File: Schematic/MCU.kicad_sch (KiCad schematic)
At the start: 21 parts, among them IC3 STM32H743VIT6, SW1 TS24CA, Y1 8MHz

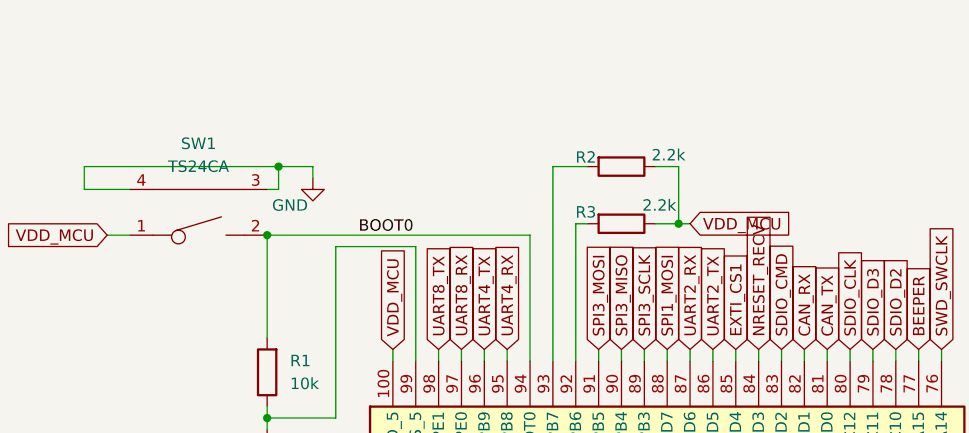
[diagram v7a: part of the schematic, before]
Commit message: update schematic after reviewing some footprints
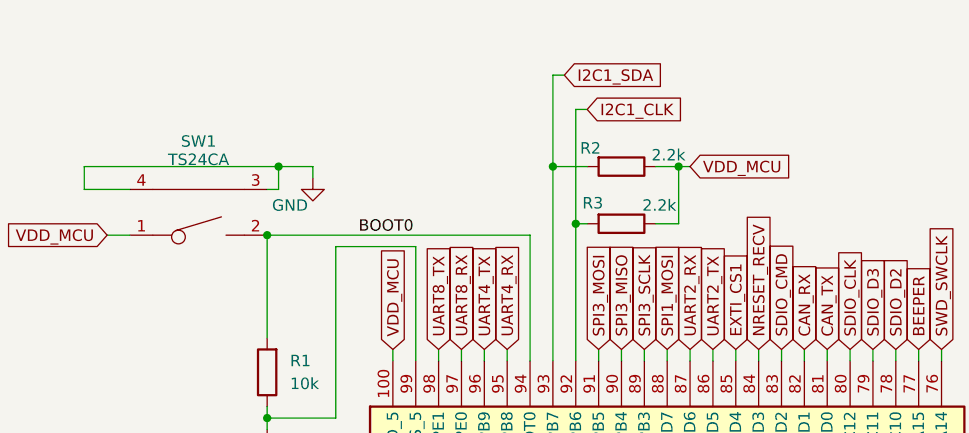
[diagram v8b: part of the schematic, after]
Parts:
- C1, C53: MPN CL10A225KB8NNNC -> (none); Manufacturer SAMSUNG -> (none)
- C2, C5, C6, C7, C8, C9: MPN 0603B104K500NT -> (none); Manufacturer FH -> (none)
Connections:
- net I2C1_SDA: now reaches IC3.93 (PB7), R2.2
- net I2C1_CLK: now reaches IC3.92 (PB6), R3.2
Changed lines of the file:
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@@
 	)
 	(junction
+		(at 88.9 29.21)
+		(diameter 0)
+		(color 0 0 0 0)
+	)
+	(junction
 		(at 58.42 29.21)
 		(diameter 0)
@@
 	)
 	(junction
+		(at 102.87 29.21)
+		(diameter 0)
+		(color 0 0 0 0)
+	)
+	(junction
 		(at 220.98 30.48)
 		(diameter 0)
@@
 	)
 	(junction
+		(at 91.44 35.56)
+		(diameter 0)
+		(color 0 0 0 0)
+	)
+	(junction
 		(at 127 158.75)
 		(diameter 0)
@@
 	)
 	(junction
-		(at 102.87 35.56)
-		(diameter 0)
-		(color 0 0 0 0)
-	)
-	(junction
 		(at 45.72 101.6)
 		(diameter 0)
@@
 	(wire
 		(pts
-			(xy 102.87 35.56) (xy 104.14 35.56)
-		)
-		(stroke
-			(width 0)
-			(type default)
-		)
-	)
-	(wire
-		(pts
 			(xy 139.7 106.68) (xy 140.97 106.68)
 		)
@@
 	(wire
 		(pts
+			(xy 91.44 22.86) (xy 91.44 35.56)
+		)
+		(stroke
+			(width 0)
+			(type default)
+		)
+	)
+	(wire
+		(pts
 			(xy 71.12 148.59) (xy 71.12 149.86)
 		)
@@
 	(wire
 		(pts
+			(xy 88.9 19.05) (xy 88.9 29.21)
+		)
+		(stroke
+			(width 0)
+			(type default)
+		)
+	)
+	(wire
+		(pts
 			(xy 130.81 148.59) (xy 127 148.59)
 		)
@@
 	(wire
 		(pts
+			(xy 92.71 22.86) (xy 91.44 22.86)
+		)
+		(stroke
+			(width 0)
+			(type default)
+		)
+	)
+	(wire
+		(pts
+			(xy 102.87 29.21) (xy 104.14 29.21)
+		)
+		(stroke
+			(width 0)
+			(type default)
+		)
+	)
+	(wire
+		(pts
 			(xy 124.46 179.07) (xy 121.92 179.07)
 		)
@@
 	(wire
 		(pts
+			(xy 90.17 19.05) (xy 88.9 19.05)
+		)
+		(stroke
+			(width 0)
+			(type default)
+		)
+	)
+	(wire
+		(pts
 			(xy 228.6 125.73) (xy 228.6 133.35)
 		)
@@
 		)
 	)
+	(global_label "I2C1_SDA"
+		(shape input)
+		(at 90.17 19.05 0)
+		(fields_autoplaced yes)
+		(effects
+			(font
+				(size 1.27 1.27)
+			)
+			(justify left)
+		)
+		(property "Intersheetrefs" "${INTERSHEET_REFS}"
+			(at 101.9847 19.05 0)
+			(effects
+				(font
+					(size 1.27 1.27)
+				)
+				(justify left)
+				(hide yes)
+			)
+		)
+	)
 	(global_label "NRST"
 		(shape input)
@@
 		)
 	)
+	(global_label "I2C1_CLK"
+		(shape input)
+		(at 92.71 22.86 0)
+		(fields_autoplaced yes)
+		(effects
+			(font
+				(size 1.27 1.27)
+			)
+			(justify left)
+		)
+		(property "Intersheetrefs" "${INTERSHEET_REFS}"
+			(at 104.5247 22.86 0)
+			(effects
+				(font
+					(size 1.27 1.27)
+				)
+				(justify left)
+				(hide yes)
+			)
+		)
+	)
 	(global_label "SPI1_MOSI"
 		(shape input)
@@
 	(global_label "VDD_MCU"
 		(shape input)
-		(at 104.14 35.56 0)
+		(at 104.14 29.21 0)
 		(fields_autoplaced yes)
 		(effects
@@
 		)
 		(property "Intersheetrefs" "${INTERSHEET_REFS}"
-			(at 115.7733 35.56 0)
+			(at 115.7733 29.21 0)
 			(effects
 				(font
@@
 			)
 		)
-		(property "Datasheet" "https://www.lcsc.com/datasheet/C30926.pdf"
+		(property "Datasheet" ""
 			(at 45.72 107.95 0)
 			(effects
@@
 			)
 		)
-		(property "MPN" "0603B104K500NT "
+		(property "MPN" ""
 			(at 45.72 107.95 0)
 			(effects
@@
 			)
 		)
-		(property "Manufacturer" "FH"
+		(property "Manufacturer" ""
 			(at 45.72 107.95 0)
 			(effects
@@
 			)
 		)
-		(property "Datasheet" "https://www.lcsc.com/datasheet/C30926.pdf"
+		(property "Datasheet" ""
 			(at 220.98 34.29 0)
 			(effects
@@
 			)
 		)
-		(property "MPN" "0603B104K500NT "
+		(property "MPN" ""
 			(at 220.98 34.29 0)
 			(effects
@@
 			)
 		)
-		(property "Manufacturer" "FH"
+		(property "Manufacturer" ""
 			(at 220.98 34.29 0)
 			(effects
@@
 			)
 		)
-		(property "Datasheet" "https://www.samsungsem.com/resources/file/global/support/product_catalog/MLCC.pdf"
+		(property "Datasheet" ""
 			(at 163.83 73.66 0)
 			(effects
@@
 			)
 		)
-		(property "MPN" "CL10A225KB8NNNC"
+		(property "MPN" ""
 			(at 163.83 73.66 90)
 			(effects
@@
 			)
 		)
-		(property "Manufacturer" "SAMSUNG"
+		(property "Manufacturer" ""
 			(at 163.83 73.66 90)
 			(effects
@@
 			)
 		)
-		(property "Datasheet" "https://www.lcsc.com/datasheet/C30926.pdf"
+		(property "Datasheet" ""
 			(at 232.41 34.29 0)
 			(effects
@@
 			)
 		)
-		(property "MPN" "0603B104K500NT "
+		(property "MPN" ""
 			(at 232.41 34.29 0)
 			(effects
@@
 			)
 		)
-		(property "Manufacturer" "FH"
+		(property "Manufacturer" ""
 			(at 232.41 34.29 0)
 			(effects
@@
 		(dnp no)
 		(property "Reference" "R2"
-			(at 93.726 28.194 90)
+			(at 94.234 27.178 90)
 			(effects
 				(font
@@
 		(on_board yes)
 		(dnp no)
-		(fields_autoplaced yes)
 		(property "Reference" "SW1"
-			(at 49.53 26.67 0)
+			(at 49.53 26.416 0)
 			(effects
 				(font
@@
 		)
 		(property "Value" "TS24CA"
-			(at 49.53 29.21 0)
+			(at 49.53 28.448 0)
 			(effects
 				(font
@@
 			)
 		)
-		(property "Datasheet" "https://www.lcsc.com/datasheet/C30926.pdf"
+		(property "Datasheet" ""
 			(at 243.84 34.29 0)
 			(effects
@@
 			)
 		)
-		(property "MPN" "0603B104K500NT "
+		(property "MPN" ""
 			(at 243.84 34.29 0)
 			(effects
@@
 			)
 		)
-		(property "Manufacturer" "FH"
+		(property "Manufacturer" ""
 			(at 243.84 34.29 0)
 			(effects
@@
 		(dnp no)
 		(property "Reference" "R3"
-			(at 93.726 34.29 90)
+			(at 94.488 33.274 90)
 			(effects
 				(font
@@
 			)
 		)
-		(property "Datasheet" "https://www.lcsc.com/datasheet/C30926.pdf"
+		(property "Datasheet" ""
 			(at 198.12 34.29 0)
 			(effects
@@
 			)
 		)
-		(property "MPN" "0603B104K500NT "
+		(property "MPN" ""
 			(at 198.12 34.29 0)
 			(effects
@@
 			)
 		)
-		(property "Manufacturer" "FH"
+		(property "Manufacturer" ""
 			(at 198.12 34.29 0)
 			(effects
@@
 			)
 		)
-		(property "Datasheet" "https://www.lcsc.com/datasheet/C30926.pdf"
+		(property "Datasheet" ""
 			(at 209.55 34.29 0)
 			(effects
@@
 			)
 		)
-		(property "MPN" "0603B104K500NT "
+		(property "MPN" ""
 			(at 209.55 34.29 0)
 			(effects
@@
 			)
 		)
-		(property "Manufacturer" "FH"
+		(property "Manufacturer" ""
 			(at 209.55 34.29 0)
 			(effects
@@
 			)
 		)
-		(property "Datasheet" "https://www.samsungsem.com/resources/file/global/support/product_catalog/MLCC.pdf"
+		(property "Datasheet" ""
 			(at 127 152.4 0)
 			(effects
@@
 			)
 		)
-		(property "MPN" "CL10A225KB8NNNC"
+		(property "MPN" ""
 			(at 127 152.4 0)
 			(effects
@@
 			)
 		)
-		(property "Manufacturer" "SAMSUNG"
+		(property "Manufacturer" ""
 			(at 127 152.4 0)
 			(effects
